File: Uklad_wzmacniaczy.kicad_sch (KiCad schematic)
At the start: 88 parts, among them J1 SJ1-3523N, J2 MEM2080-00-128-00-A, J3 Conn_01x10_Pin, U1 OPA2388IDR, U10 AD5162BRMZ10-RL7, U11 AD5162BRMZ10-RL7, U12 LT3094EMSE-TRPBF, U2 REF2033QDDCRQ1, U3 AD8421ARMZ, U4 OPA388IDR, U5 AD8421ARMZ, U6 TPD4E1B06DRLR, U7 AD5162BRMZ10-RL7, U8 LT3042EMSE-TRPBF, U9 TPS65135RTER

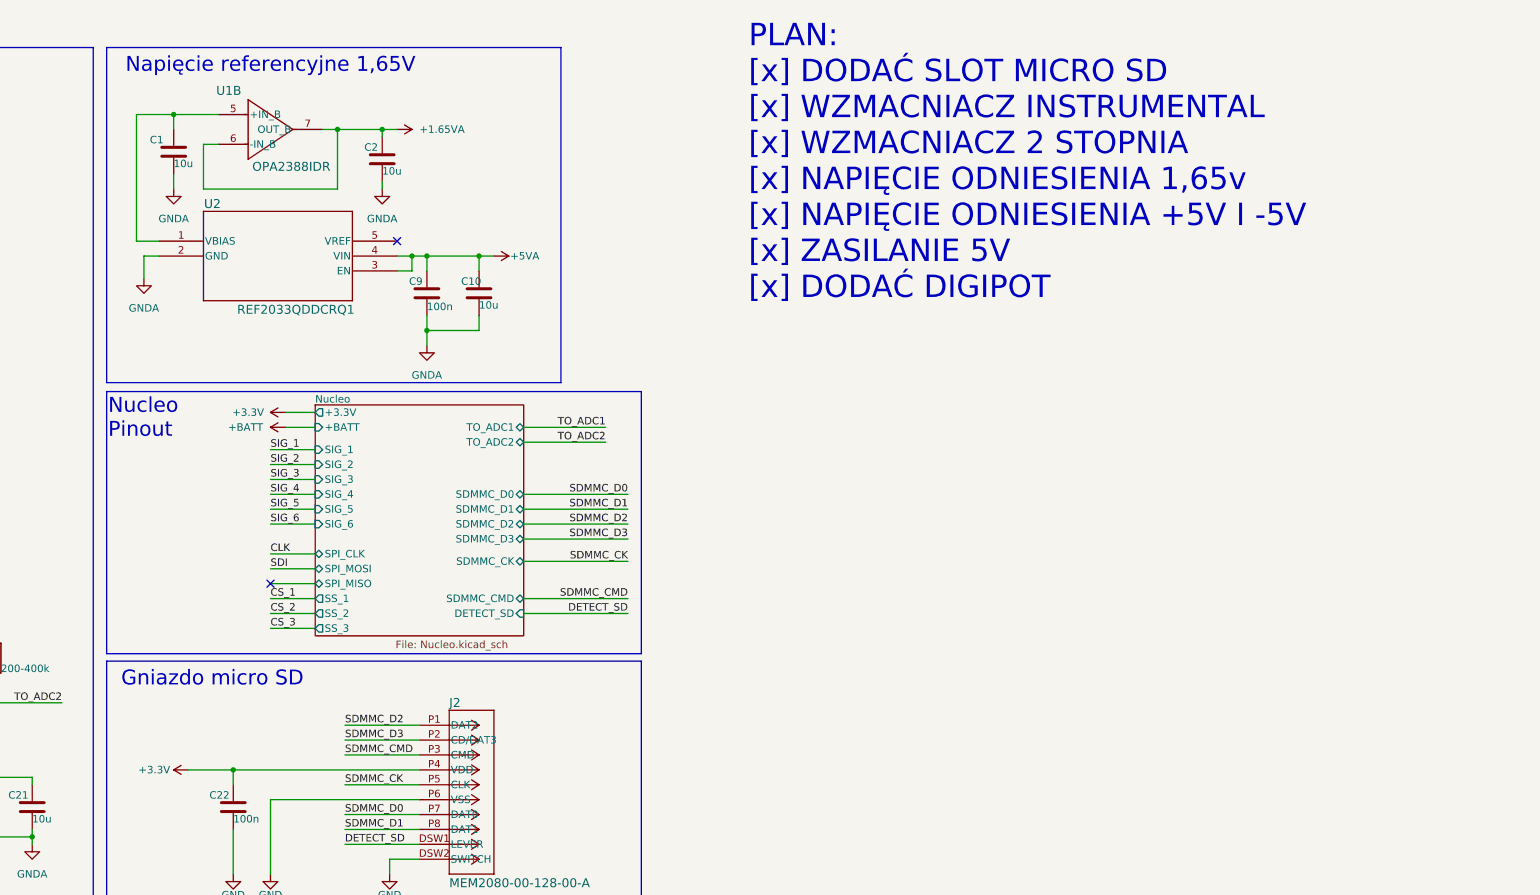
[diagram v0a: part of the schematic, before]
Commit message: Errors in pcb layout removed, footprints fixed, microvias changed to regular vias
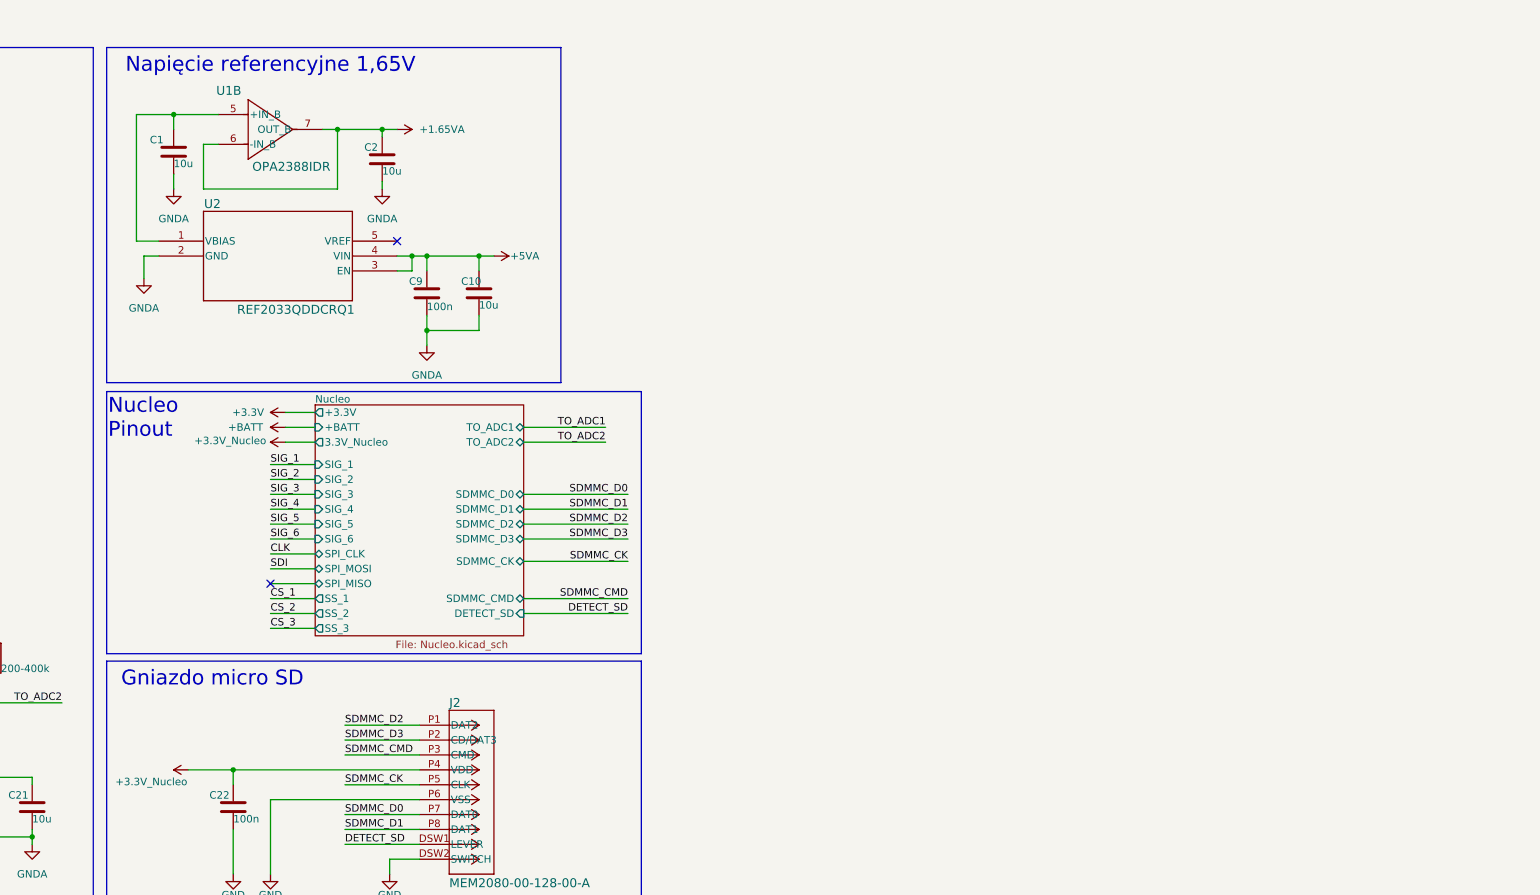
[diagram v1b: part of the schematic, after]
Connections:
- net +3.3V: no longer C22.1, J2.P4 (VDD)
- new net +3.3V_Nucleo: C22.1, J2.P4 (VDD)
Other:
- sheet Nucleo ports: added 3.3V_Nucleo; removed none
- note removed: "PLAN: [x] DODAĆ SLOT MICRO SD [x] WZMACNIACZ INSTRUMENTAL [x] WZMACNIACZ 2 STOPNIA [x] NAPIĘCIE ODNIESIENIA 1,65v [x] NAPIĘCIE ODNIESIENIA +5V I -5V [x] ZASILANIE 5V [x] DODAĆ DIGIPOT"
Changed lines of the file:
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@@
 		)
 	)
-	(text "PLAN:\n[x] DODAĆ SLOT MICRO SD\n[x] WZMACNIACZ INSTRUMENTAL\n[x] WZMACNIACZ 2 STOPNIA\n[x] NAPIĘCIE ODNIESIENIA 1,65v\n[x] NAPIĘCIE ODNIESIENIA +5V I -5V\n[x] ZASILANIE 5V\n[x] DODAĆ DIGIPOT\n"
-		(exclude_from_sim no)
-		(at 424.434 36.068 0)
-		(effects
-			(font
-				(size 3.81 3.81)
-			)
-			(justify left)
-		)
-	)
 	(junction
 		(at 250.19 40.64)
@@
 	(wire
 		(pts
-			(xy 342.9 95.25) (xy 350.52 95.25)
+			(xy 342.9 97.79) (xy 350.52 97.79)
 		)
 		(stroke
@@
 	(wire
 		(pts
-			(xy 342.9 97.79) (xy 350.52 97.79)
+			(xy 342.9 100.33) (xy 350.52 100.33)
 		)
 		(stroke
@@
 	(wire
 		(pts
+			(xy 345.44 83.82) (xy 350.52 83.82)
+		)
+		(stroke
+			(width 0)
+			(type default)
+		)
+	)
+	(wire
+		(pts
 			(xy 259.08 50.8) (xy 259.08 52.07)
 		)
@@
 	(wire
 		(pts
-			(xy 342.9 87.63) (xy 350.52 87.63)
+			(xy 342.9 90.17) (xy 350.52 90.17)
 		)
 		(stroke
@@
 	(wire
 		(pts
-			(xy 342.9 92.71) (xy 350.52 92.71)
+			(xy 342.9 95.25) (xy 350.52 95.25)
 		)
 		(stroke
@@
 	(wire
 		(pts
-			(xy 342.9 90.17) (xy 350.52 90.17)
+			(xy 342.9 92.71) (xy 350.52 92.71)
 		)
 		(stroke
@@
 	(wire
 		(pts
-			(xy 342.9 85.09) (xy 350.52 85.09)
+			(xy 342.9 87.63) (xy 350.52 87.63)
 		)
 		(stroke
@@
 	)
 	(label "SIG_1"
-		(at 342.9 85.09 0)
+		(at 342.9 87.63 0)
 		(effects
 			(font
@@
 	)
 	(label "SIG_4"
-		(at 342.9 92.71 0)
+		(at 342.9 95.25 0)
 		(effects
 			(font
@@
 	)
 	(label "SIG_3"
-		(at 342.9 90.17 0)
+		(at 342.9 92.71 0)
 		(effects
 			(font
@@
 	)
 	(label "SIG_5"
-		(at 342.9 95.25 0)
+		(at 342.9 97.79 0)
 		(effects
 			(font
@@
 	)
 	(label "SIG_2"
-		(at 342.9 87.63 0)
+		(at 342.9 90.17 0)
 		(effects
 			(font
@@
 	)
 	(label "SIG_6"
-		(at 342.9 97.79 0)
+		(at 342.9 100.33 0)
 		(effects
 			(font
@@
 			)
 		)
-		(property "Datasheet" ""
+		(property "Datasheet" "https://www.digikey.pl/pl/products/detail/texas-instruments/tpd4e1b06drlr/4878711"
 			(at 101.6 142.24 0)
 			(hide yes)
@@
 	)
 	(symbol
+		(lib_id "power:+3.3V")
+		(at 345.44 83.82 90)
+		(unit 1)
+		(body_style 1)
+		(exclude_from_sim no)
+		(in_bom yes)
+		(on_board yes)
+		(in_pos_files yes)
+		(dnp no)
+		(property "Reference" "#PWR096"
+			(at 349.25 83.82 0)
+			(hide yes)
+			(show_name no)
+			(do_not_autoplace no)
+			(effects
+				(font
+					(size 1.27 1.27)
+				)
+			)
+		)
+		(property "Value" "+3.3V_Nucleo"
+			(at 336.042 83.566 90)
+			(show_name no)
+			(do_not_autoplace no)
+			(effects
+				(font
+					(size 1.27 1.27)
+				)
+			)
+		)
+		(property "Footprint" ""
+			(at 345.44 83.82 0)
+			(hide yes)
+			(show_name no)
+			(do_not_autoplace no)
+			(effects
+				(font
+					(size 1.27 1.27)
+				)
+			)
+		)
+		(property "Datasheet" ""
+			(at 345.44 83.82 0)
+			(hide yes)
+			(show_name no)
+			(do_not_autoplace no)
+			(effects
+				(font
+					(size 1.27 1.27)
+				)
+			)
+		)
+		(property "Description" "Power symbol creates a global label with name \"+3.3V\""
+			(at 345.44 83.82 0)
+			(hide yes)
+			(show_name no)
+			(do_not_autoplace no)
+			(effects
+				(font
+					(size 1.27 1.27)
+				)
+			)
+		)
+		(pin "1"
+		)
+		(instances
+			(project "Uklad_wzmacniaczy"
+				(path "/5beef803-c264-4e64-a820-2636d42e5954"
+					(reference "#PWR096")
+					(unit 1)
+				)
+			)
+		)
+	)
+	(symbol
 		(lib_id "Connector:TestPoint")
 		(at 36.83 111.76 270)
@@
 			)
 		)
-		(property "Value" "+3.3V"
-			(at 323.088 139.7 90)
+		(property "Value" "+3.3V_Nucleo"
+			(at 322.58 141.732 90)
 			(show_name no)
 			(do_not_autoplace no)
@@
 		)
 		(pin "SIG_1" input
-			(at 350.52 85.09 180)
+			(at 350.52 87.63 180)
 			(effects
 				(font
@@
 		)
 		(pin "SIG_3" input
-			(at 350.52 90.17 180)
+			(at 350.52 92.71 180)
 			(effects
 				(font
@@
 		)
 		(pin "SIG_4" input
-			(at 350.52 92.71 180)
+			(at 350.52 95.25 180)
 			(effects
 				(font
@@
 		)
 		(pin "SIG_5" input
-			(at 350.52 95.25 180)
+			(at 350.52 97.79 180)
 			(effects
 				(font
@@
 		)
 		(pin "SIG_2" input
-			(at 350.52 87.63 180)
+			(at 350.52 90.17 180)
 			(effects
 				(font
@@
 		)
 		(pin "SIG_6" input
-			(at 350.52 97.79 180)
+			(at 350.52 100.33 180)
 			(effects
 				(font
@@
 			(effects
 				(font
+					(size 1.27 1.27)
+				)
+				(justify left)
+			)
+		)
+		(pin "3.3V_Nucleo" output
+			(at 350.52 83.82 180)
+			(effects
+				(font
